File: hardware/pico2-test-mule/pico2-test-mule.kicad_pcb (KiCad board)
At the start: 2 copper layers, 52.5 x 42 mm, 70 parts, among them J2 SPEAKER, J4 POWER, J5 EXT_CAP, J6 RAILS, J7 AUX, J8 MOTOR, Q1 DMN2991UDA-7B, Q10 SS8050, Q11 SS8050, Q12 SS8050, Q13 SS8050, Q2 DMN2991UDA-7B, Q3 NST847BPDP6T5G, Q4 NST847BPDP6T5G, Q5 DMN2991UDA-7B, Q6 DMN2991UDA-7B, Q7 DMN2991UDA-7B, Q8 DMN2991UDA-7B, Q9 SS8050, U1 NCS2220AMUT1G, U2 AP63203WU, U5 MAX98357AEWL+T, U6 MD9927, U7 PICO

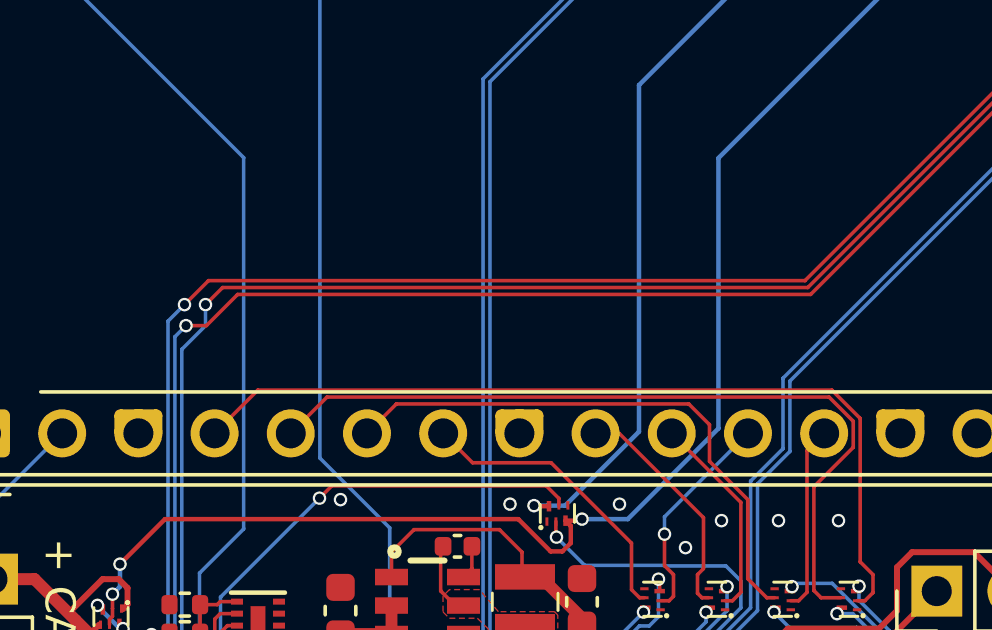
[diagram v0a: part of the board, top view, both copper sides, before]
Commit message: chore: reorder i2s gpios
chore: add qr code to silkscreen
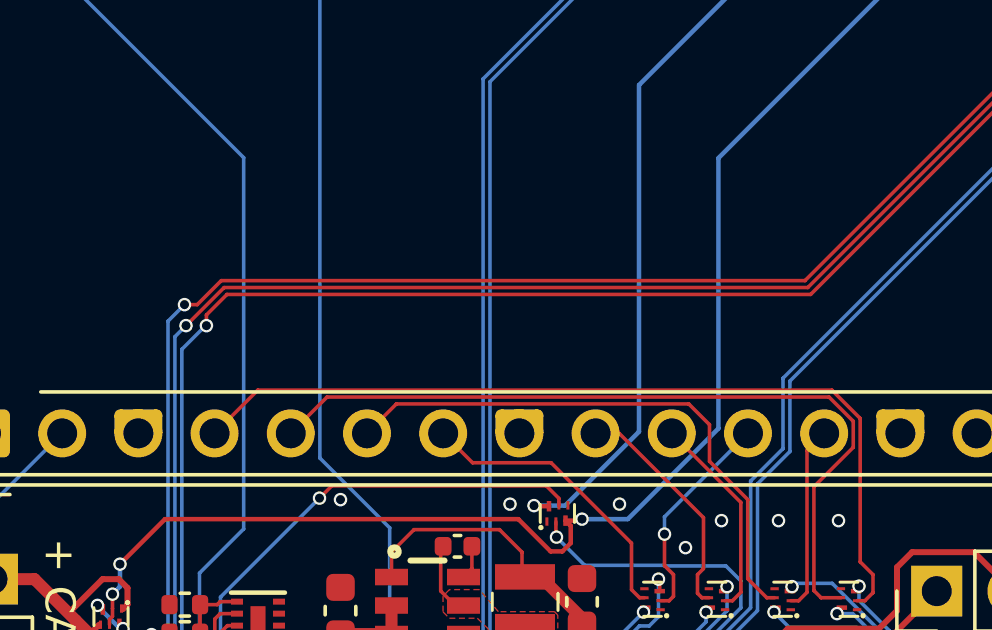
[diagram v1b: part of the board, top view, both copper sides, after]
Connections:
- U7 pad 24: /I2S_BCLK -> /I2S_DIN
- U7 pad 25: /I2S_DIN -> /I2S_BCLK
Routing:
- net /I2S_BCLK: track 58.5 -> 55.9 mm
- net /I2S_DIN: track 56.3 -> 58.7 mm

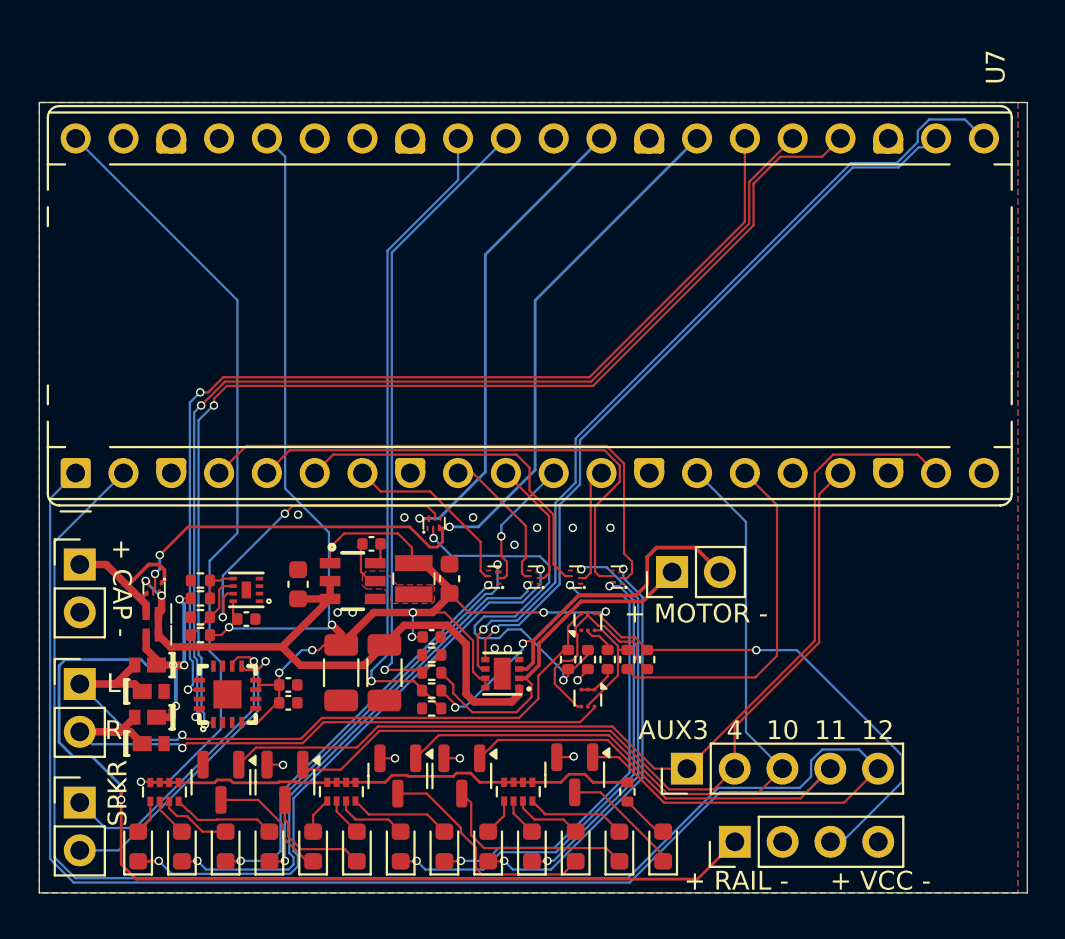
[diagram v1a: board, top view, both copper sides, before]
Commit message: chore: add hardware revision and date codes
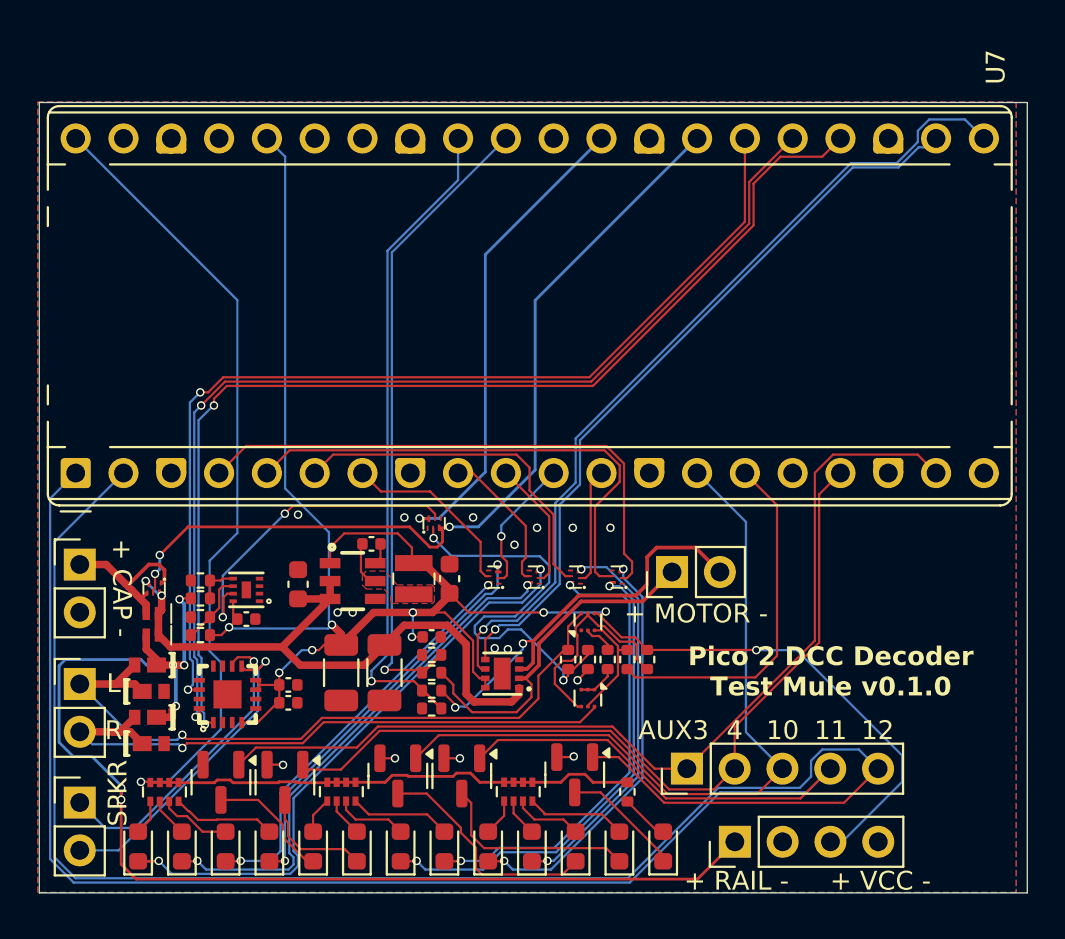
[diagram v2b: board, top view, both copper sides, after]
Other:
- board text added: "Pico 2 DCC Decoder Test Mule ${REVISION}"
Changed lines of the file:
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@@
 	)
 	(paper "A4")
+	(title_block
+		(date "2025-02-16")
+		(rev "v0.1.0")
+	)
 	(layers
 		(0 "F.Cu" signal)
@@
 		)
 	)
+	(gr_text "Pico 2 DCC Decoder\nTest Mule ${REVISION}"
+		(at 130.21 68.89 0)
+		(layer "F.SilkS")
+		(effects
+			(font
+				(size 1 1)
+				(thickness 0.2)
+				(bold yes)
+			)
+		)
+	)
 	(gr_text "11"
 		(at 130.2 72.6 0)
@@
 		(polygon
 			(pts
-				(xy 88.15 38.65) (xy 140.15 38.65) (xy 140.15 80.65) (xy 88.15 80.65)
+				(xy 88.06 38.63) (xy 140.06 38.63) (xy 140.06 80.63) (xy 88.06 80.63)
 			)
 		)
